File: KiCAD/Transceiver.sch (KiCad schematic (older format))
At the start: 5 parts

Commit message: Add mcu
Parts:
- removed Q?: Q_NPN_BCE, Package_TO_SOT_SMD:SOT-323_SC-70_Handsoldering, symbol Device:Q_NPN_BCE
- added R? (x2): R, symbol Device:R
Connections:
- net labels added: AM_Out, BF_IN_AM, FBBFin, FBBFout
- wire segments 18 -> 24
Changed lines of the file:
@@
 $Descr A4 11693 8268
 encoding utf-8
-Sheet 1 5
+Sheet 1 6
 Title "AM & FM Transceiver"
 Date ""
@@
 Nota: Vcc 4.5-8.0v
 $Sheet
-S 3500 1100 1150 200
+S 3600 1550 1150 200
 U 5E70F6BF
 F0 "Si5351 atenuator" 50
 F1 "Si5351_Filter.sch" 50
-F2 "Clk0_Fi" I L 3500 1200 50
-F3 "Clk0_Fo" I R 4650 1200 50
+F2 "Clk0_Fi" I L 3600 1650 50
+F3 "Clk0_Fo" I R 4750 1650 50
 $EndSheet
 Wire Wire Line
@@
 F1 "MCU.sch" 50
 $EndSheet
-Text Label 3500 1200 2    50   ~ 0
+Text Label 3600 1650 2    50   ~ 0
 Clk0_Fi
-Text Label 4650 1200 0    50   ~ 0
+Text Label 4750 1650 0    50   ~ 0
 Clk0_Fo
 Text Notes 1000 1150 0    50   ~ 0
@@
 Text Label 2350 3700 0    50   ~ 0
 MClk_Fi
-$Sheet
-S 3500 3500 1100 300
-U 5E71DA61
-F0 "AD9833 Filter" 50
-F1 "AD98333 filter.sch" 50
-F2 "MClk_Fi" I L 3500 3600 50
-F3 "IN_A_Out" I R 4600 3600 50
-F4 "IN_B_Out" I R 4600 3700 50
-$EndSheet
 Text Label 6950 1300 2    50   ~ 0
 IN_A_Out
 Text Label 6950 1400 2    50   ~ 0
 IN_B_Out
-Text Label 4600 3600 0    50   ~ 0
-IN_A_Out
-Text Label 4600 3700 0    50   ~ 0
-IN_B_Out
-Text Label 3500 3600 2    50   ~ 0
-MClk_Fi
 Text Label 1300 3600 2    50   ~ 0
 SS_AD9833
@@
 Text Label 5850 7100 2    50   ~ 0
 SAI_FS
-Text Notes 4550 3450 0    50   ~ 0
+Text Notes 5700 3350 0    50   ~ 0
 Nota : IN_A & IN_B are biased internally, They are symmetrical.\nEquivalent AC impédance 1.5Khos 3pF 50MHz.\n
-$Comp
-L Device:Q_NPN_BCE Q?
-U 1 1 5E76FBFD
-P 9700 1750
-F 0 "Q?" H 9891 1796 50  0000 L CNN
-F 1 "Q_NPN_BCE" H 9891 1705 50  0000 L CNN
-F 2 "Package_TO_SOT_SMD:SOT-323_SC-70_Handsoldering" H 9900 1850 50  0001 C CNN
-F 3 "~" H 9700 1750 50  0001 C CNN
-	1    9700 1750
-	1    0    0    -1
-$EndComp
-$Sheet
-S 3650 5550 1150 350
+$Sheet
+S 7300 5450 1150 450
 U 5E77AF45
 F0 "AM Module" 50
 F1 "AM Module.sch" 50
-F2 "HF" I L 3650 5800 50
-F3 "BF" I L 3650 5700 50
-F4 "Feed_BackBFin" I R 4800 5700 50
-F5 "Feed_BackBFout" I R 4800 5800 50
+F2 "HF" I L 7300 5700 50
+F3 "BF" I L 7300 5600 50
+F4 "Feed_BackBFin" I R 8450 5600 50
+F5 "Feed_BackBFout" I R 8450 5700 50
 $EndSheet
 Wire Wire Line
@@
 Text Label 2400 1600 0    50   ~ 0
 Clk1_Fi
-Text Label 3650 5800 2    50   ~ 0
+Text Label 7300 5700 2    50   ~ 0
 Clk1_Fi
+Text Label 5850 7600 2    50   ~ 0
+FBBFin
+Text Label 5850 7500 2    50   ~ 0
+FBBFout
+Text Label 8450 5600 0    50   ~ 0
+FBBFin
+Text Label 8450 5700 0    50   ~ 0
+FBBFout
+Text Label 4650 3500 2    50   ~ 0
+MClk_Fi
+Text Label 5750 3500 0    50   ~ 0
+IN_A_Out
+$Sheet
+S 4650 3400 1100 200
+U 5E71DA61
+F0 "AD9833 Filter" 50
+F1 "AD98333 filter.sch" 50
+F2 "MClk_Fi" I L 4650 3500 50
+F3 "IN_A_Out" O R 5750 3500 50
+$EndSheet
+Text HLabel 8450 5800 0    50   Input ~ 0
+AM_Out
+Text Label 8450 5800 0    50   ~ 0
+AM_Out
+Text Label 7300 5600 2    50   ~ 0
+BF_IN_AM
+Text Label 5500 5550 0    50   ~ 0
+BF_IN_AM
+Text Label 4950 5650 2    50   ~ 0
+OutL
+Text Label 4950 5550 2    50   ~ 0
+OutR
+$Comp
+L Device:R R?
+U 1 1 5E7DE6C9
+P 5200 5550
+F 0 "R?" V 4993 5550 50  0000 C CNN
+F 1 "R" V 5084 5550 50  0000 C CNN
+F 2 "" V 5130 5550 50  0001 C CNN
+F 3 "~" H 5200 5550 50  0001 C CNN
+	1    5200 5550
+	0    1    1    0
+$EndComp
+$Comp
+L Device:R R?
+U 1 1 5E7DEE26
+P 5200 5650
+F 0 "R?" V 4993 5650 50  0000 C CNN
+F 1 "R" V 5084 5650 50  0000 C CNN
+F 2 "" V 5130 5650 50  0001 C CNN
+F 3 "~" H 5200 5650 50  0001 C CNN
+	1    5200 5650
+	0    -1   -1   0
+$EndComp
+Wire Wire Line
+	5500 5550 5450 5550
+Wire Wire Line
+	5350 5650 5450 5650
+Wire Wire Line
+	5450 5650 5450 5550
+Connection ~ 5450 5550
+Wire Wire Line
+	5450 5550 5350 5550
+Wire Wire Line
+	4950 5650 5050 5650
+Wire Wire Line
+	4950 5550 5050 5550
+$Sheet
+S 5200 4350 1150 250
+U 5E7F5958
+F0 "LEDS" 50
+F1 "LEDs_indicators.sch" 50
+$EndSheet
 $EndSCHEMATC

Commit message: Add MCU module and other modules
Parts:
- removed U?: Si5351A-B-GT, Package_SO:MSOP-10_3x3mm_P0.5mm, symbol Oscillator:Si5351A-B-GT
- removed U?: AD9833, symbol SA612A:AD9833
- removed U?: PCM5102, Package_SO:TSSOP-20_4.4x6.5mm_P0.65mm, symbol Audio:PCM5102
- added J?: Conn_01x04_Female, symbol Connector:Conn_01x04_Female
- added J? (x2): Conn_01x20_Female, symbol Connector:Conn_01x20_Female
- added J? (x2): Conn_01x07_Female, Connector_PinSocket_2.54mm:PinSocket_1x07_P2.54mm_Vertical, symbol Connector:Conn_01x07_Female
- added J? (x2): Conn_01x06_Female, symbol Connector:Conn_01x06_Female
- added J?: Conn_01x08_Female, symbol Connector:Conn_01x08_Female
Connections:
- net labels added: GY-PCM5102, I2C3_SCL, I2C3_SDA, I2Sa_CK, I2Sa_SD, I2Sa_WS, I2Sb_CK, I2Sb_SD, I2Sb_WS, LED, Nokia_DC, Nokia_Light, Nokia_RST, SPI5_MOSI, SPI5_NSS, SPI5_SCK, USART1_RX, USART1_TX, USART2_RX, USART2_TX
- net labels removed: SAI_FS, SAI_MCLK, SAI_SCK, SAI_SD
- wire segments 24 -> 29
- no-connect marks 1 -> 4
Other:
- note added: "3.3V"
- note added: "5V"
- note added: "BCK"
- note added: "CE"
- note added: "CLK"
- note added: "DC"
- note added: "DIN"
- note added: "GND"
- note added: "LCK"
- note added: "LIGHT"
- note added: "LR"
- note added: "PA0"
- note added: "PA1"
- note added: "PA10"
- note added: "PA11"
- note added: "PA12"
- note added: "PA15"
- note added: "PA2"
- note added: "PA3"
- note added: "PA4"
- note added: "PA5"
- note added: "PA6"
- note added: "PA7"
- note added: "PA8"
- note added: "PA9"
- note added: "PB0"
- note added: "PB1"
- note added: "PB10"
- note added: "PB12"
- note added: "PB13"
- note added: "PB14"
- note added: "PB15"
- note added: "PB2"
- note added: "PB3"
- note added: "PB4"
- note added: "PB5"
- note added: "PB6"
- note added: "PB7"
- note added: "PB8"
- note added: "PB9"
- note added: "PC13"
- note added: "PC14"
- note added: "PC15"
- note added: "RST"
- note added: "SCK"
- note added: "SCK_CLK"
- note added: "SD_DATA"
- note added: "VB"
- note added: "VCC"
- note added: "WS_L/R"
- note removed: "Nota : IN_A & IN_B are biased internally, They are symmetrical.\nEquivalent AC impédance 1.5Khos 3pF 50MHz.\n"
- note removed: "Nota : replaced by PCM5102A\nUSE a board ?"
- note removed: "Nota: Vcc 3.3v"
- moved on the sheet: R?

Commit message: Just save files Begin PCB
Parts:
- added J10, J9: Conn_01x04_Female, Connector_PinHeader_2.54mm:PinHeader_1x04_P2.54mm_Vertical, symbol Connector:Conn_01x04_Female
- added J11: Conn_01x03_Female, Connector_PinHeader_2.54mm:PinHeader_1x03_P2.54mm_Vertical, symbol Connector:Conn_01x03_Female
- added J12, J13: Conn_Coaxial, Connector_Coaxial:SMA_Amphenol_132289_EdgeMount, symbol Connector:Conn_Coaxial
- J1, J7: renamed from J?; footprint (none) -> Connector_PinSocket_2.54mm:PinSocket_1x20_P2.54mm_Vertical
- J4, J6: renamed from J?; footprint (none) -> Connector_PinHeader_2.54mm:PinHeader_1x06_P2.54mm_Vertical
- J5: renamed from J?; footprint (none) -> Connector_PinHeader_2.54mm:PinHeader_1x04_P2.54mm_Vertical
- J8: renamed from J?; footprint (none) -> Connector_PinHeader_2.54mm:PinHeader_1x08_P2.54mm_Vertical
- R1, R2: renamed from R?; footprint (none) -> Resistor_SMD:R_0805_2012Metric
- U1: renamed from U?; footprint (none) -> Package_DIP:DIP-8_W7.62mm
- gave numbers to parts that had none: 2
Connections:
- net +3V3: now also J1.3 (Pin_3), J7.1 (Pin_1), J11.1 (Pin_1)
- net +5V: now also J10.1 (Pin_1), J9.1 (Pin_1)
- net AM_Out: now also J13.1 (In)
- net GND: now also J10.4 (Pin_4), J11.3 (Pin_3), J12.2 (Ext), J13.2 (Ext), J9.4 (Pin_4)
- net Nokia_DC: now also J7.19 (Pin_19)
- net Nokia_Light: now also J7.15 (Pin_15)
- net Nokia_RST: now also J7.18 (Pin_18)
- net USART1_RX: now also J9.2 (Pin_2)
- net USART1_TX: now also J7.7 (Pin_7), J9.3 (Pin_3); no longer J7.15 (Pin_15)
- net USART2_RX: now also J10.2 (Pin_2)
- net USART2_TX: now also J10.3 (Pin_3)
- net RST: now reaches J1.16 (Pin_16)
- net IR_IN: now reaches J1.5 (Pin_5)
- net IR_IN: now also J11.2 (Pin_2)
- net I2C3_SCL renamed SCL_1
- net I2C3_SDA renamed SDA_1
- no-connect marks 4 -> 6
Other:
- note added: "Lout"
- note added: "Rout"

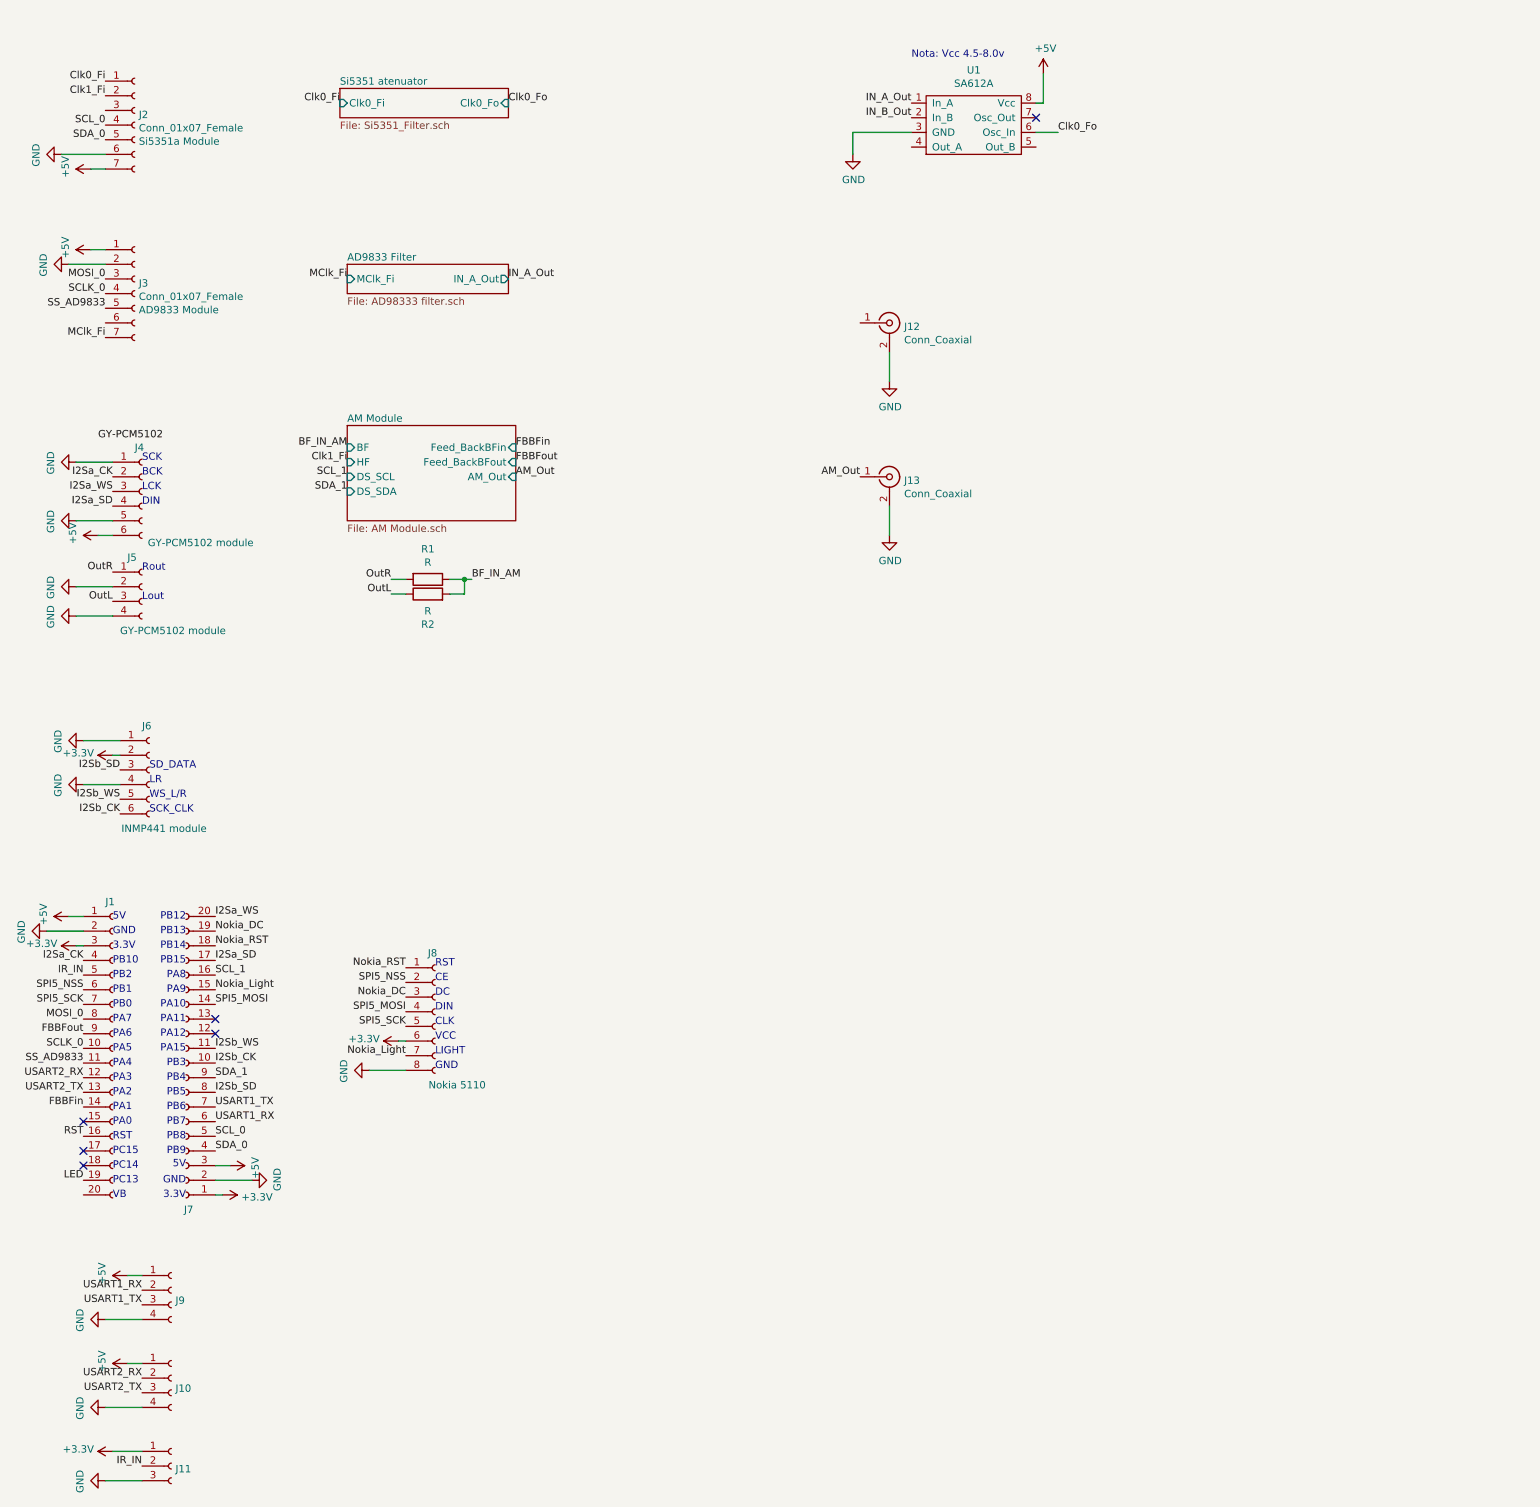
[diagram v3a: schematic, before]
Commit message: Make PCB and change NPN and PNP for AM output
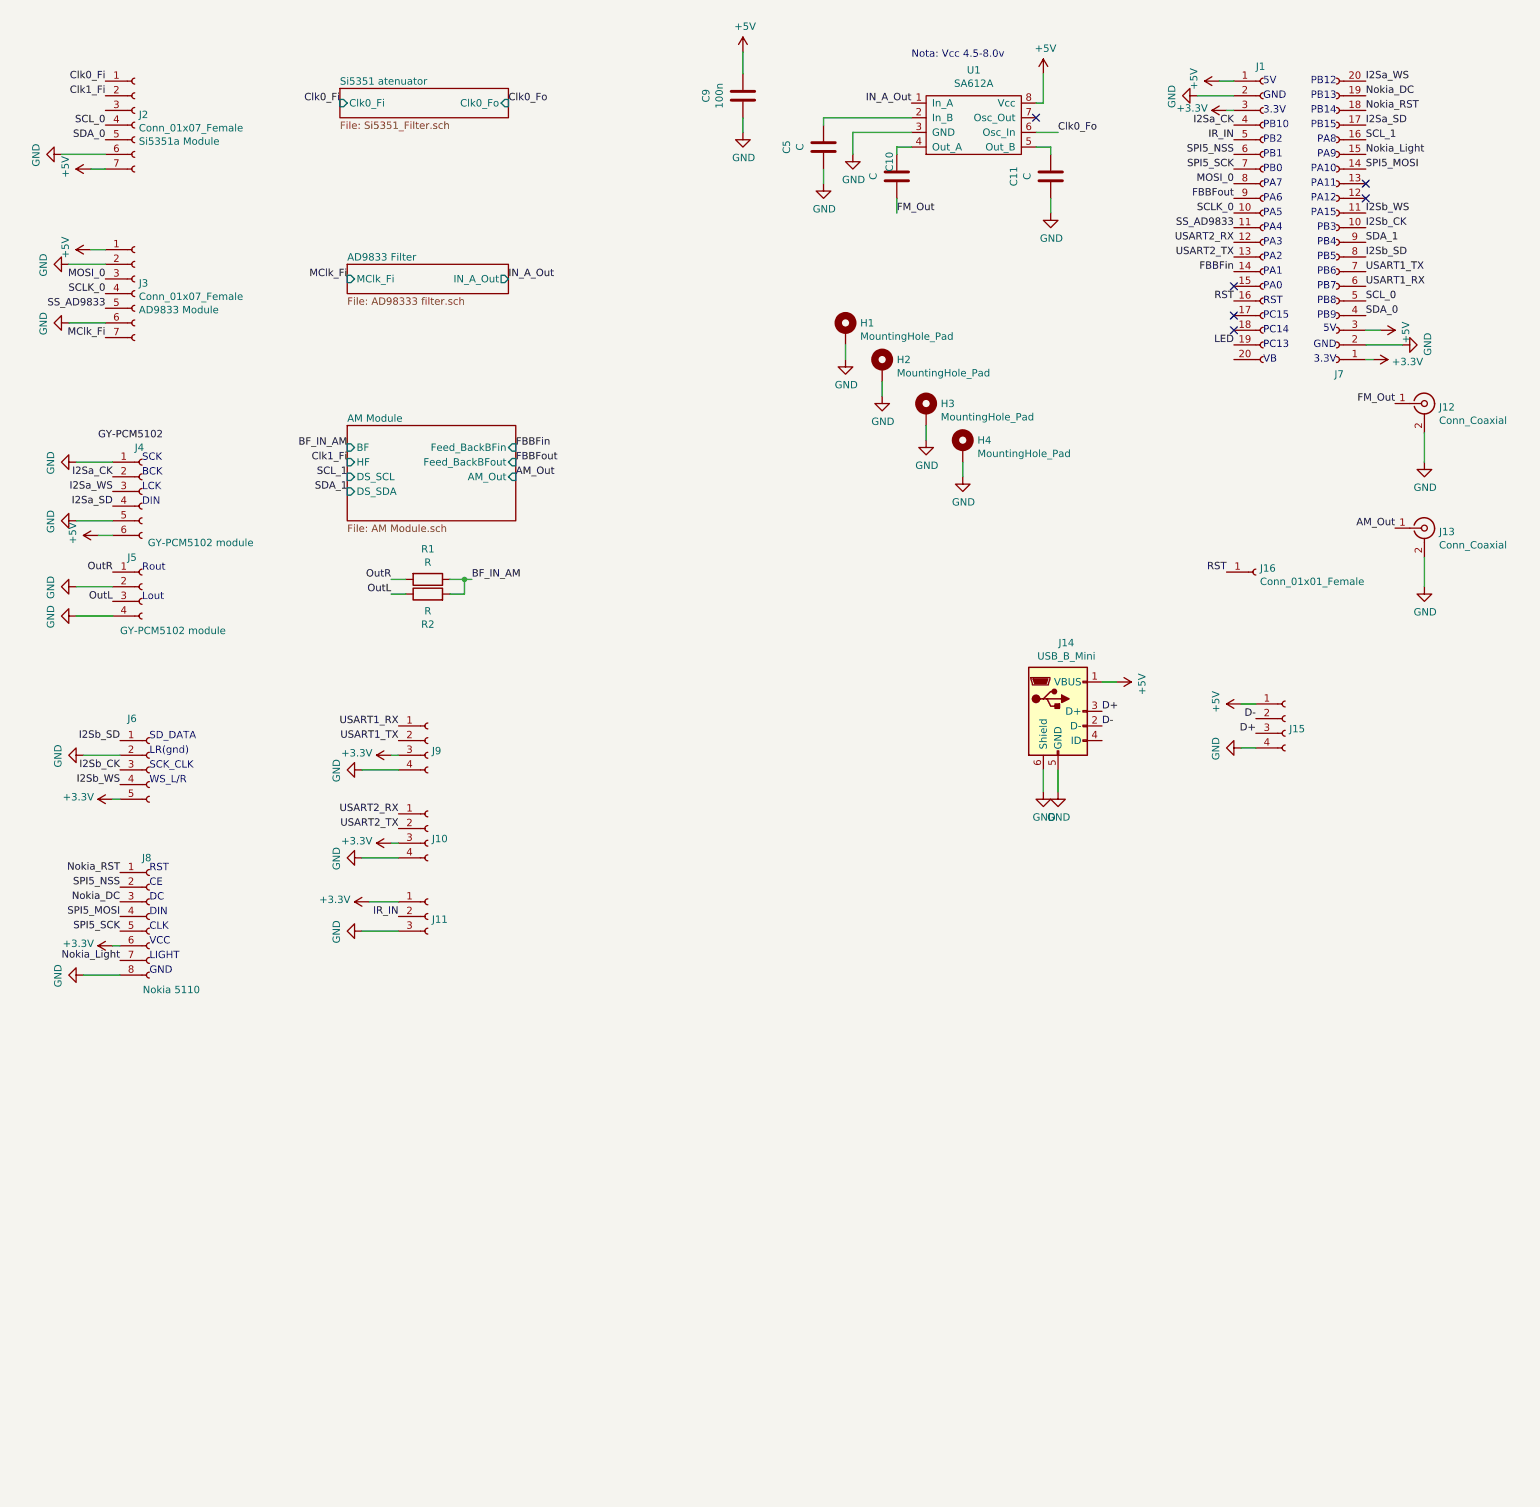
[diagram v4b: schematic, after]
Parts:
- removed J6: Conn_01x06_Female, Connector_PinHeader_2.54mm:PinHeader_1x06_P2.54mm_Vertical, symbol Connector:Conn_01x06_Female
- added C10, C11, C5: C, Capacitor_SMD:C_0805_2012Metric, symbol Device:C
- added C9: 100n, Capacitor_SMD:C_0805_2012Metric, symbol Device:C
- added H1, H2, H3, H4: MountingHole_Pad, MountingHole:MountingHole_2.7mm_M2.5_Pad_Via, symbol Mechanical:MountingHole_Pad
- added J14: USB_B_Mini, Connector_USB:USB_Mini-B_Lumberg_2486_01_Horizontal, symbol Connector:USB_B_Mini
- added J15: Conn_01x04_Female, Connector_PinHeader_2.54mm:PinHeader_1x04_P2.54mm_Vertical, symbol Connector:Conn_01x04_Female
- added J16: Conn_01x01_Female, Connector_PinHeader_2.54mm:PinHeader_1x01_P2.54mm_Vertical, symbol Connector:Conn_01x01_Female
- added J6: Conn_01x05_Female, Connector_PinHeader_2.54mm:PinHeader_1x05_P2.54mm_Vertical, symbol Connector:Conn_01x05_Female
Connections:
- net +3V3: now also J10.3 (Pin_3), J9.3 (Pin_3), J6.5 (Pin_5)
- net +5V: now also C9.1, J14.1 (VBUS), J15.1 (Pin_1); no longer J10.1 (Pin_1), J9.1 (Pin_1)
- net GND: now also J3.6 (Pin_6), C11.2, C5.2, C9.2, H1.1, H2.1, H3.1, H4.1, J14.5 (GND), J14.6 (Shield), J15.4 (Pin_4), J6.2 (Pin_2)
- net I2Sb_CK: now also J6.3 (Pin_3)
- net I2Sb_SD: now also J6.1 (Pin_1)
- net I2Sb_WS: now also J6.4 (Pin_4)
- net RST: now also J16.1 (Pin_1)
- net USART1_RX: now also J9.1 (Pin_1); no longer J9.2 (Pin_2)
- net USART1_TX: now also J9.2 (Pin_2); no longer J9.3 (Pin_3)
- net USART2_RX: now also J10.1 (Pin_1); no longer J10.2 (Pin_2)
- net USART2_TX: now also J10.2 (Pin_2); no longer J10.3 (Pin_3)
- net at U1.4 (Out_A): now also C10.1
- net at U1.5 (Out_B): now also C11.1
- net FM_Out: now reaches J12.1 (In)
- net FM_Out: now also C10.2
- net IN_B_Out: no longer names the net of U1.2 (In_B)
- net IN_B_Out: now also C5.1
- new net D+: J14.3 (D+), J15.3 (Pin_3)
- new net D-: J14.2 (D-), J15.2 (Pin_2)
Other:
- note added: "LR(gnd)"
- note removed: "LR"
- moved on the sheet: J1, J10, J11, J12, J13, J7, J8, J9

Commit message: Schematics and PCB update
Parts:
- removed J10: Conn_01x04_Female, Connector_PinHeader_2.54mm:PinHeader_1x04_P2.54mm_Vertical, symbol Connector:Conn_01x04_Female
- added BT1: Battery_Cell, Battery:BatteryHolder_Keystone_103_1x20mm, symbol Device:Battery_Cell
- added D1, D2: LED, LED_SMD:LED_0603_1608Metric_Castellated, symbol Device:LED
- added J10: Conn_01x05_Female, Connector_PinHeader_2.54mm:PinHeader_1x05_P2.54mm_Vertical, symbol Connector:Conn_01x05_Female
- added J17: Barrel_Jack_Switch, Connector_BarrelJack:BarrelJack_Horizontal, symbol Connector:Barrel_Jack_Switch
- added J18: Conn_01x04_Female, Connector_PinHeader_2.54mm:PinHeader_1x04_P2.54mm_Vertical, symbol Connector:Conn_01x04_Female
- added J19, J20, J21, J22, J23, J24: Conn_01x01_Female, Connector_PinHeader_2.54mm:PinHeader_1x01_P2.54mm_Vertical, symbol Connector:Conn_01x01_Female
- added Q4: 2N2219, Package_TO_SOT_THT:TO-92L_Inline_Wide, symbol Transistor_BJT:2N2219
- added R16, R17, R18: R, Resistor_SMD:R_0805_2012Metric, symbol Device:R
- added U4: AMS1117-5.0, Package_TO_SOT_SMD:SOT-223-3_TabPin2, symbol Regulator_Linear:AMS1117-5.0
- U1: footprint Package_DIP:DIP-8_W7.62mm -> Package_SO:SOIC-8-1EP_3.9x4.9mm_P1.27mm_EP2.29x3mm
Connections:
- net +3V3: now also J10.4 (Pin_4), J18.3 (Pin_3), R16.1, R17.1
- net +5V: now also J10.1 (Pin_1), J23.1 (Pin_1), U4.2 (VO)
- net Clk0_Fi: now also J2.3 (Pin_3); no longer J2.1 (Pin_1)
- net Clk1_Fi: now also J2.1 (Pin_1); no longer J2.2 (Pin_2)
- net GND: now also BT1.2 (-), J10.5 (Pin_5), J17.2, J17.3, J18.4 (Pin_4), J19.1 (Pin_1), J20.1 (Pin_1), J21.1 (Pin_1), J22.1 (Pin_1), J24.1 (Pin_1), Q4.1 (E), U4.1 (GND)
- net Nokia_Light: now also Q4.3 (C); no longer J7.15 (Pin_15)
- net SCL_1: now also J18.1 (Pin_1)
- net SDA_1: now also J18.2 (Pin_2)
- net USART2_RX: now also J10.2 (Pin_2)
- net USART2_TX: now also J10.3 (Pin_3)
- net LED2: now reaches J1.15 (Pin_15)
- net LED2: now also D1.1 (K)
- net Vbat: now reaches J1.20 (Pin_20)
- net Vbat: now also BT1.1 (+)
- net LED renamed LED1
- net LED1: now also D2.1 (K)
- new net: J17.1, U4.3 (VI)
- new net: D1.2 (A), R16.2
- new net: D2.2 (A), R17.2
- new net: Q4.2 (B), R18.2
- new net Nokia_Light_CMD: J7.15 (Pin_15), R18.1
- no-connect marks 6 -> 5
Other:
- moved on the sheet: J9
